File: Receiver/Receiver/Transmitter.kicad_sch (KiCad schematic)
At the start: 72 parts, among them J1 SSW-104-01-T-D-LL, J10 Conn_01x03, J11 Conn_01x03, J12 Conn_01x03, J13 Conn_01x03, J14 Conn_01x03, J2 105-1103-001, J3 Conn_01x06, J4 105-1103-001, J5 105-1103-001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

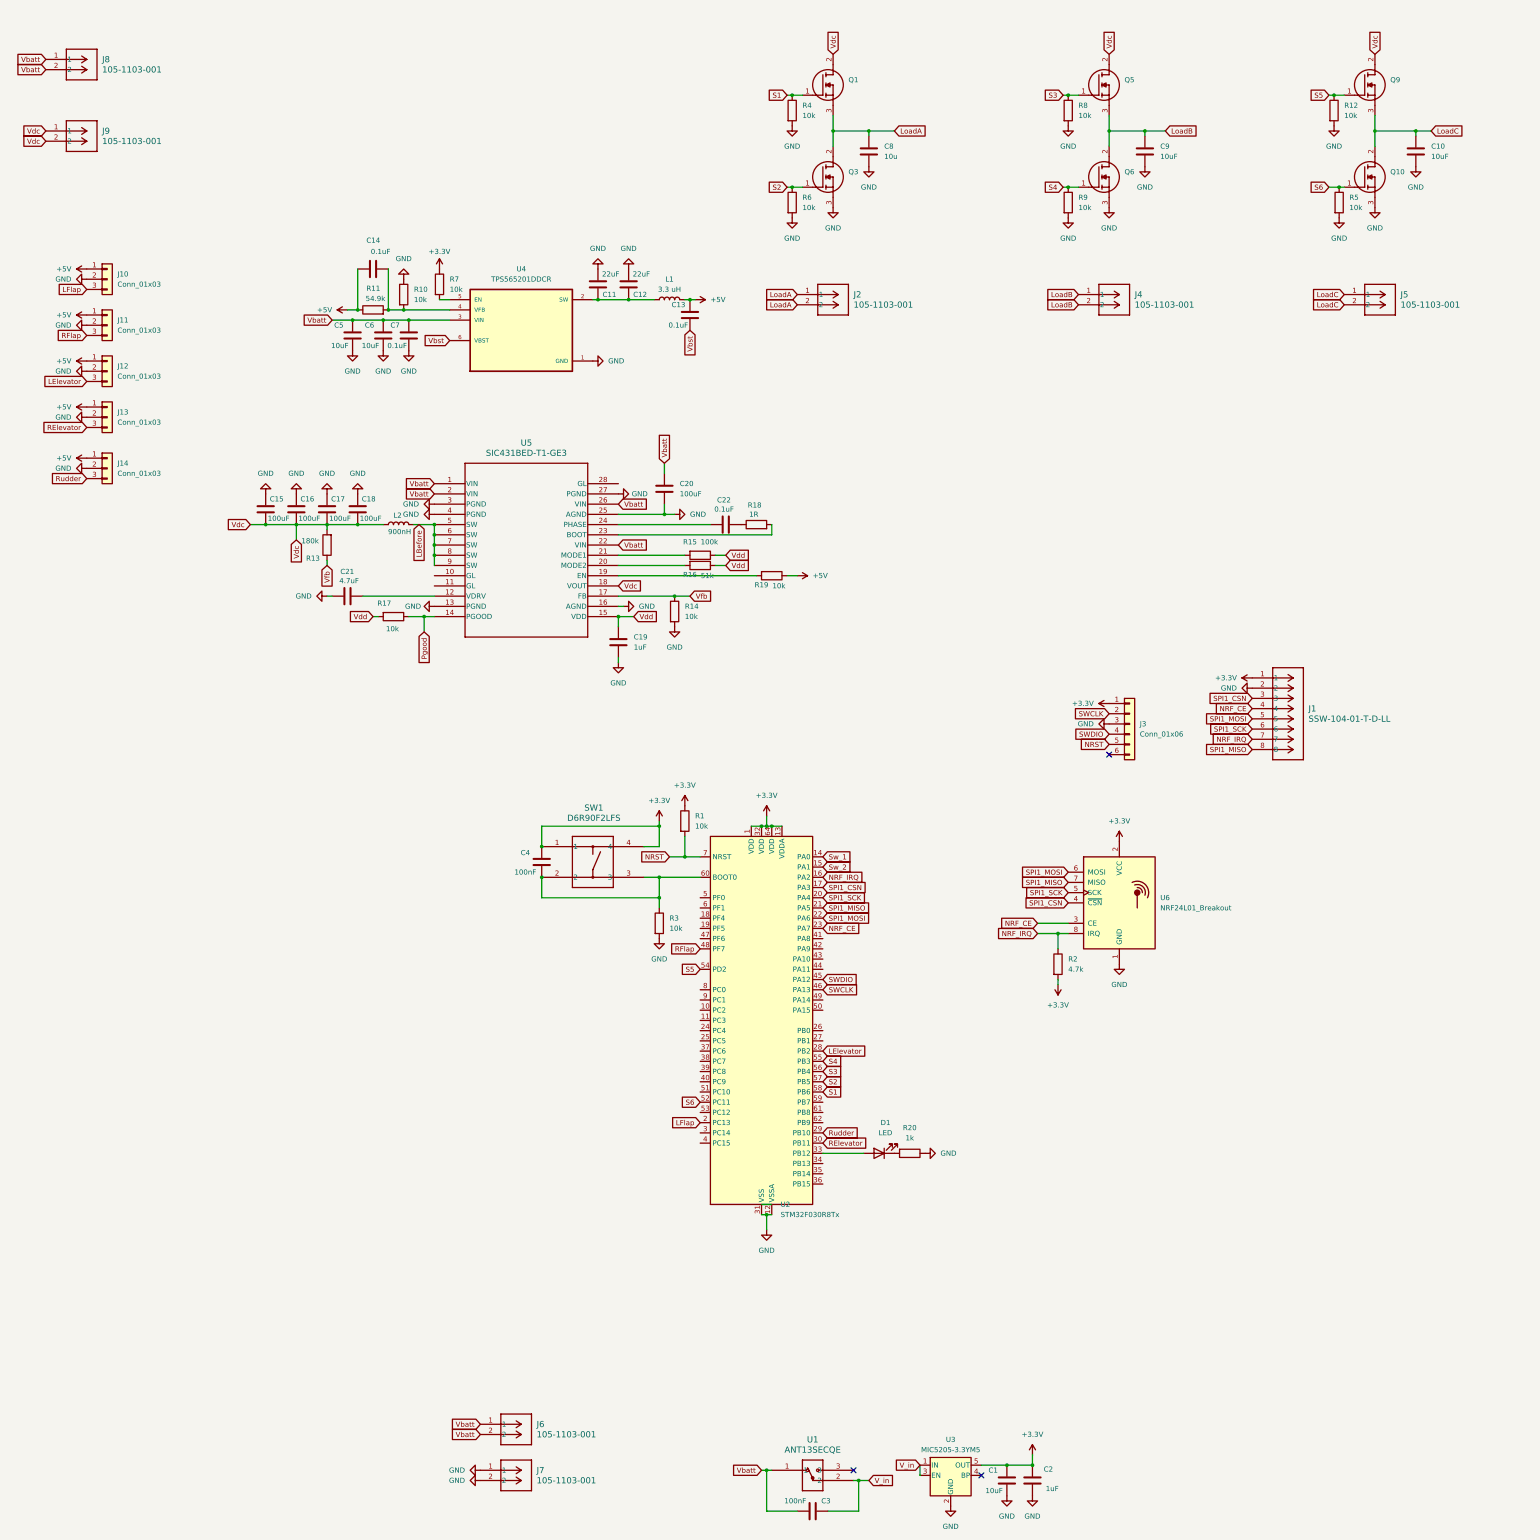
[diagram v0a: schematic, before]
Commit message: Updated KICAD files for V1, corrected SWDIO header
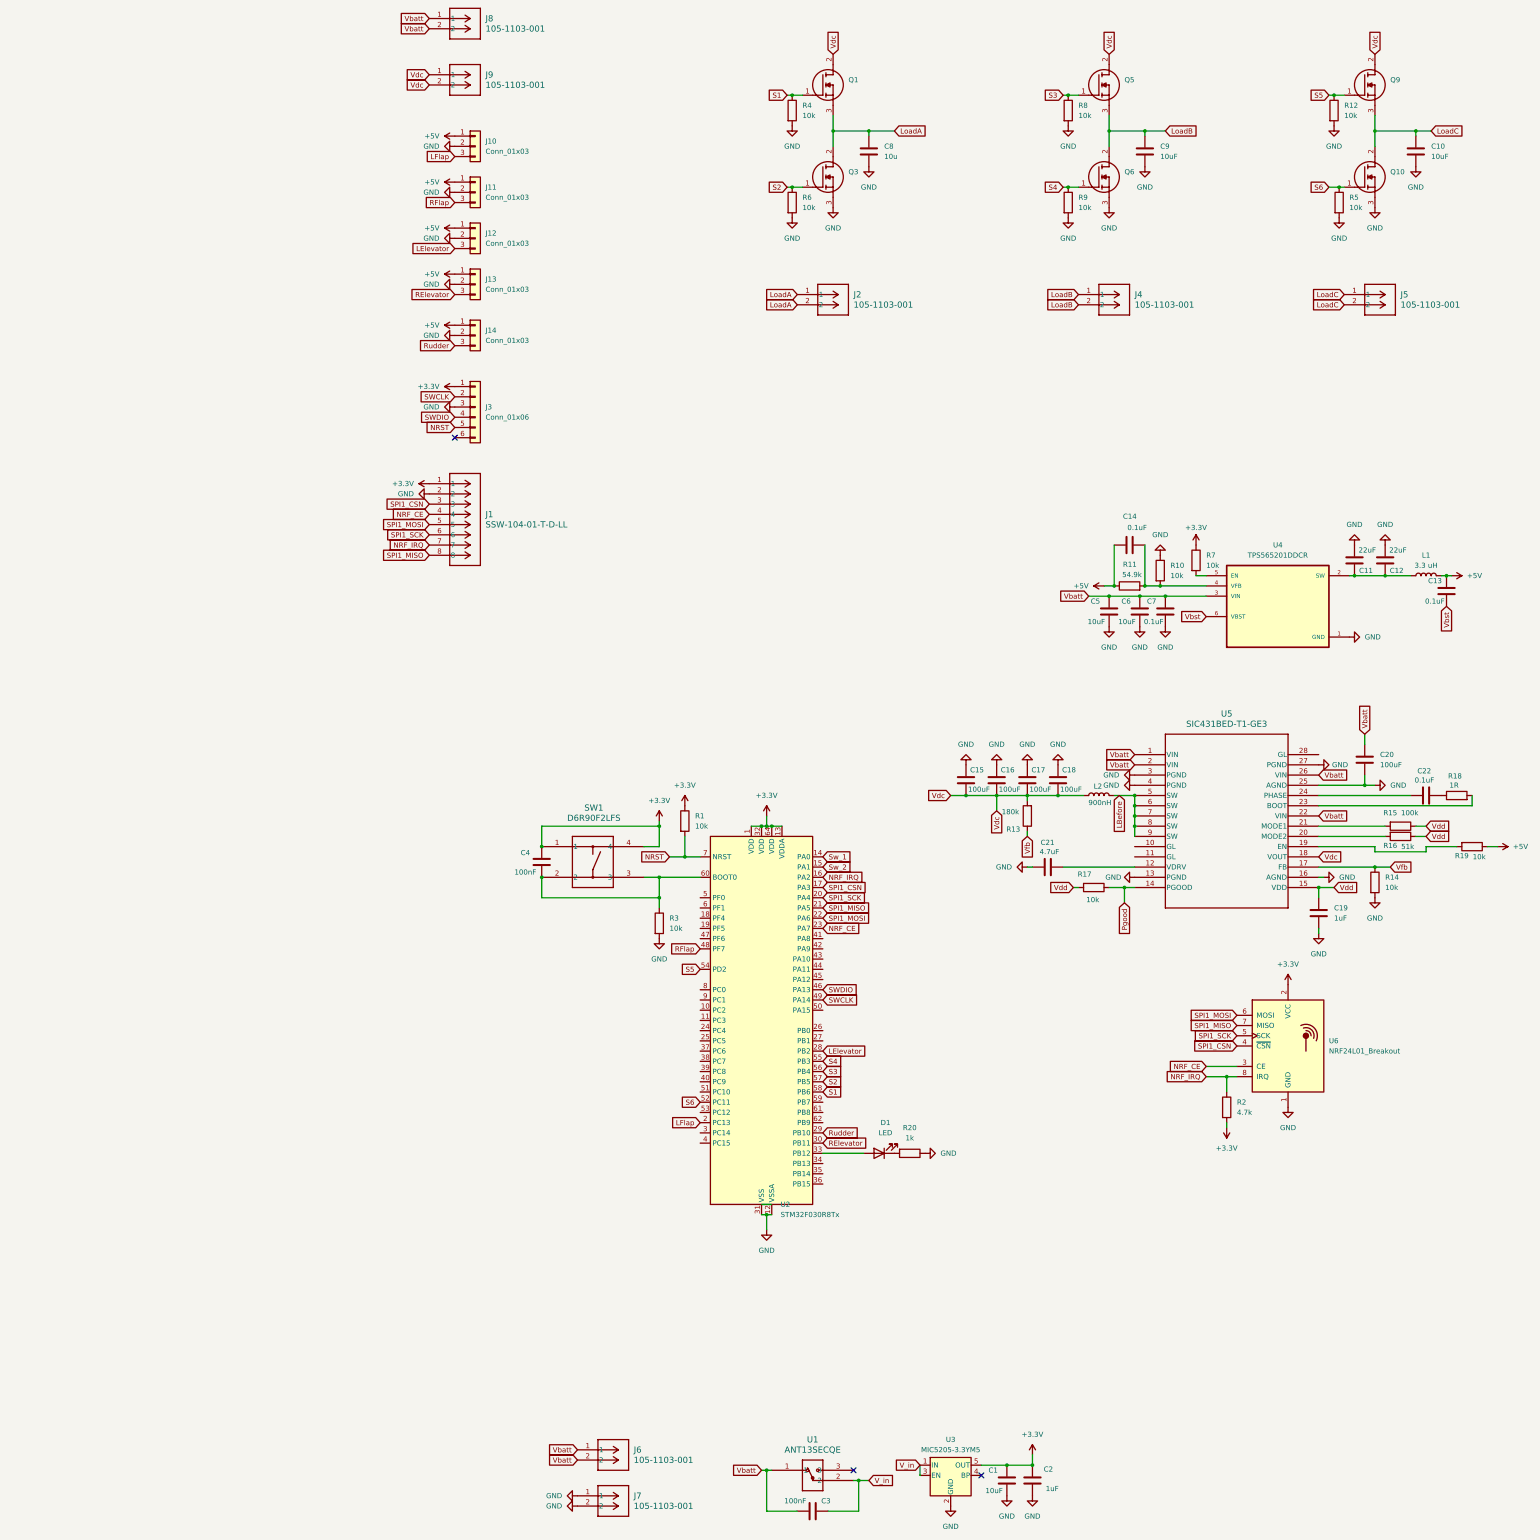
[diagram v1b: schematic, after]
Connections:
- net SWCLK: now also U2.49 (PA14); no longer U2.46 (PA13)
- net SWDIO: now also U2.46 (PA13); no longer U2.45 (PA12)
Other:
- moved on the sheet: C11, C12, C13, C14, C15, C16, C17, C18, C19, C20, C21, C22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

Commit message: PCB V2 updates
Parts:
- removed C3: 100nF, Capacitor_SMD:C_0402_1005Metric, symbol Device:C
- removed J6, J7, J8, J9: 105-1103-001, Libary1:CONN_105-1102-001, symbol BananaPlug:105-1103-001
- added C23: 0.1uF, Capacitor_SMD:C_0402_1005Metric, symbol Device:C
- added J8, J9: FCR7350R, CONN1_FCR7350R_CLF, symbol FCR7350R:FCR7350R
- added SW2: 500SSP1S2M2QEA, 500SSP1_EWI, symbol 500SSP1S2M2QEA:500SSP1S2M2QEA
- added U7: HEF4104BT_653, SO16_SOT109-1_NEX, symbol HEF4104BT:HEF4104BT_653
- C21: value 4.7uF -> 10uF
- C4: value 100nF -> 0.1uF
- R2: value 4.7k -> 10k
- U1: footprint Library2:ANT13SEC_CRS -> ANT13SEC_CRS
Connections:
- net +3.3V: now also U7.16 (VDD(A))
- net +5V: now also J10.2 (Pin_2), J11.2 (Pin_2), J12.2 (Pin_2), J13.2 (Pin_2), J14.2 (Pin_2); no longer J10.1 (Pin_1), J11.1 (Pin_1), J12.1 (Pin_1), J13.1 (Pin_1), J14.1 (Pin_1)
- net GND: now also J10.1 (Pin_1), J11.1 (Pin_1), J12.1 (Pin_1), J13.1 (Pin_1), J14.1 (Pin_1), J8.1, U7.8 (VSS); no longer J10.2 (Pin_2), J11.2 (Pin_2), J12.2 (Pin_2), J13.2 (Pin_2), J14.2 (Pin_2)
- net S1: now also U7.4 (A0); no longer Q1.1 (G), R4.1
- net S3: now also U7.5 (A1); no longer Q5.1 (G), R8.1
- net S5: now also U7.11 (A2); no longer Q9.1 (G), R12.1
- net V_in: now also C23.2
- net Vbatt: now also C23.1, J9.1, SW2.1
- net Vdc: now also SW2.2, U7.1 (VDD({B))
- net DRIVER_ENABLE: now reaches U2.41 (PA8)
- net DRIVER_ENABLE: now also U7.15 (OE)
- new net S1_BOOSTED: Q1.1 (G), R4.1, U7.3 (B0)
- new net S3_BOOSTED: Q5.1 (G), R8.1, U7.6 (B1)
- new net S5_BOOSTED: Q9.1 (G), R12.1, U7.10 (B2)
- no-connect marks 3 -> 10
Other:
- moved on the sheet: C1, C2, U3

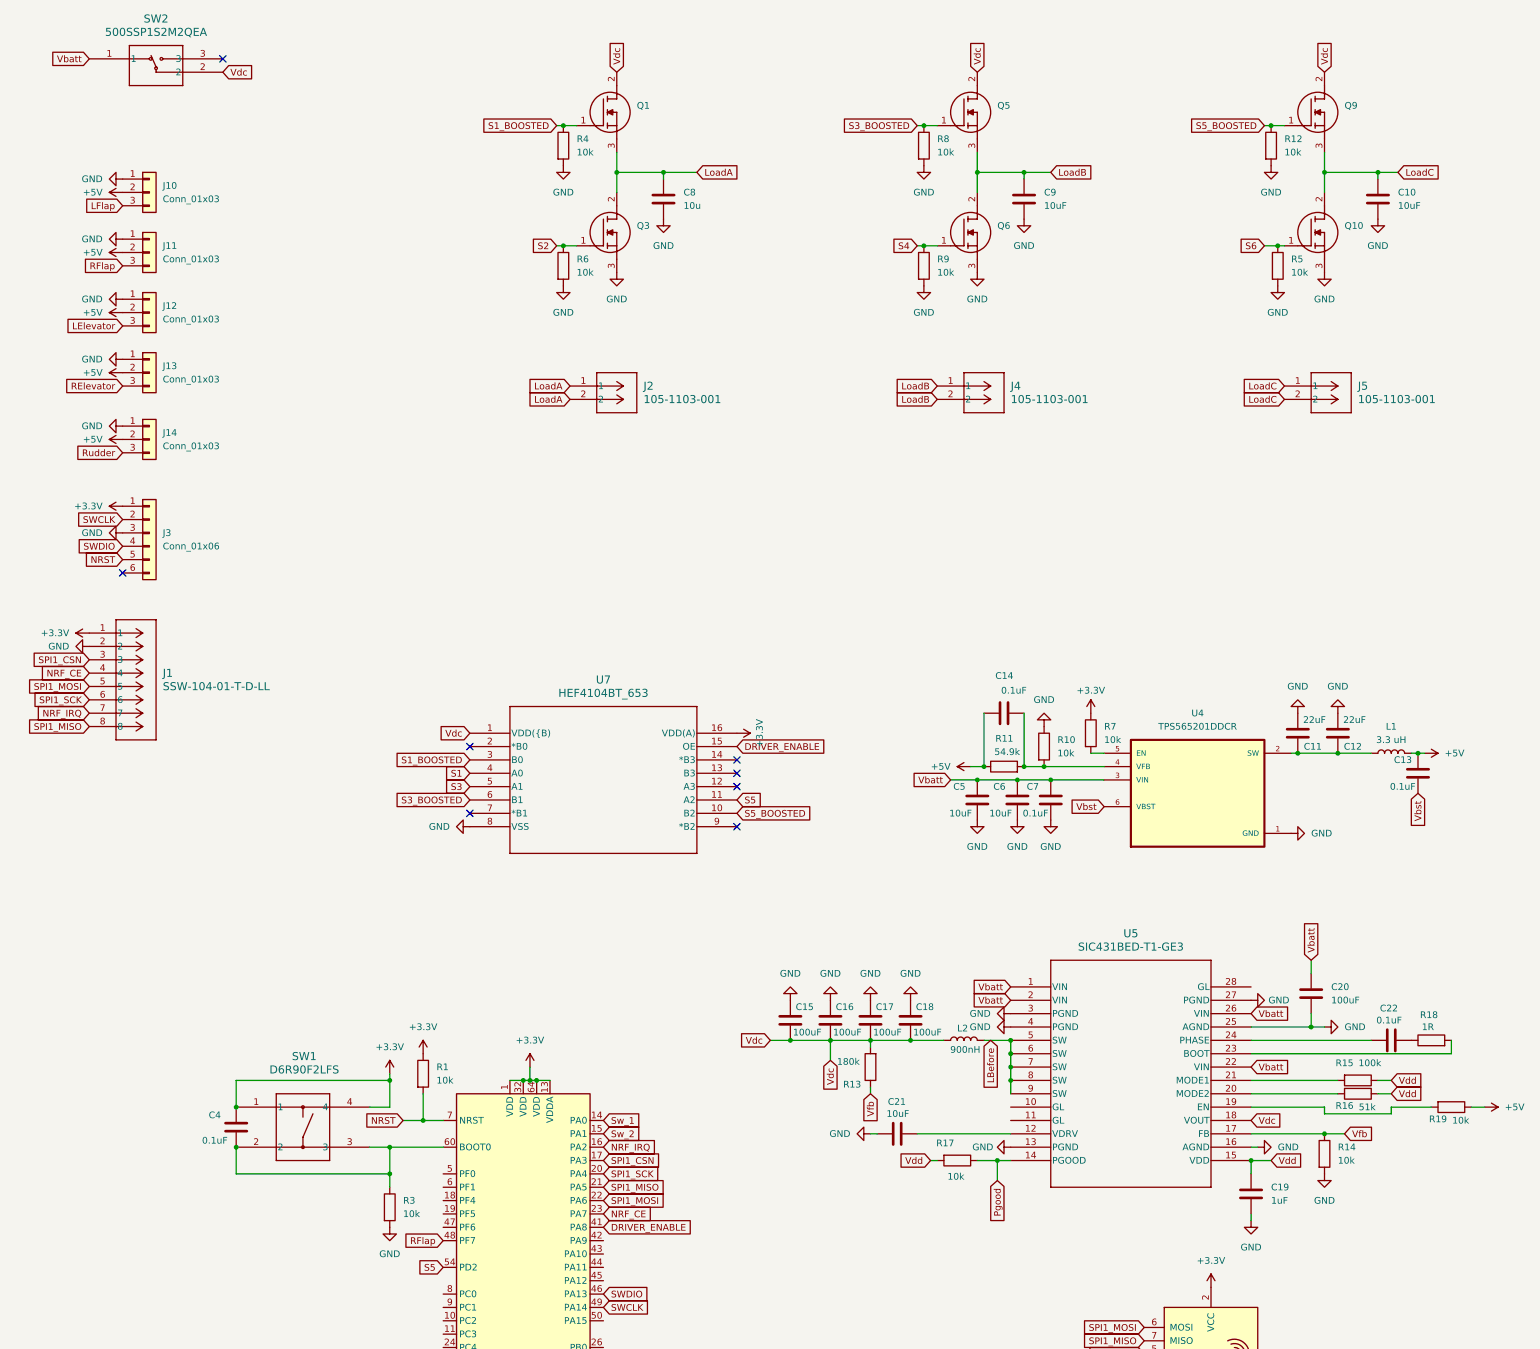
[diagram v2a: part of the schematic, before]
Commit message: Removed extra voltage converter and rerouted PCB
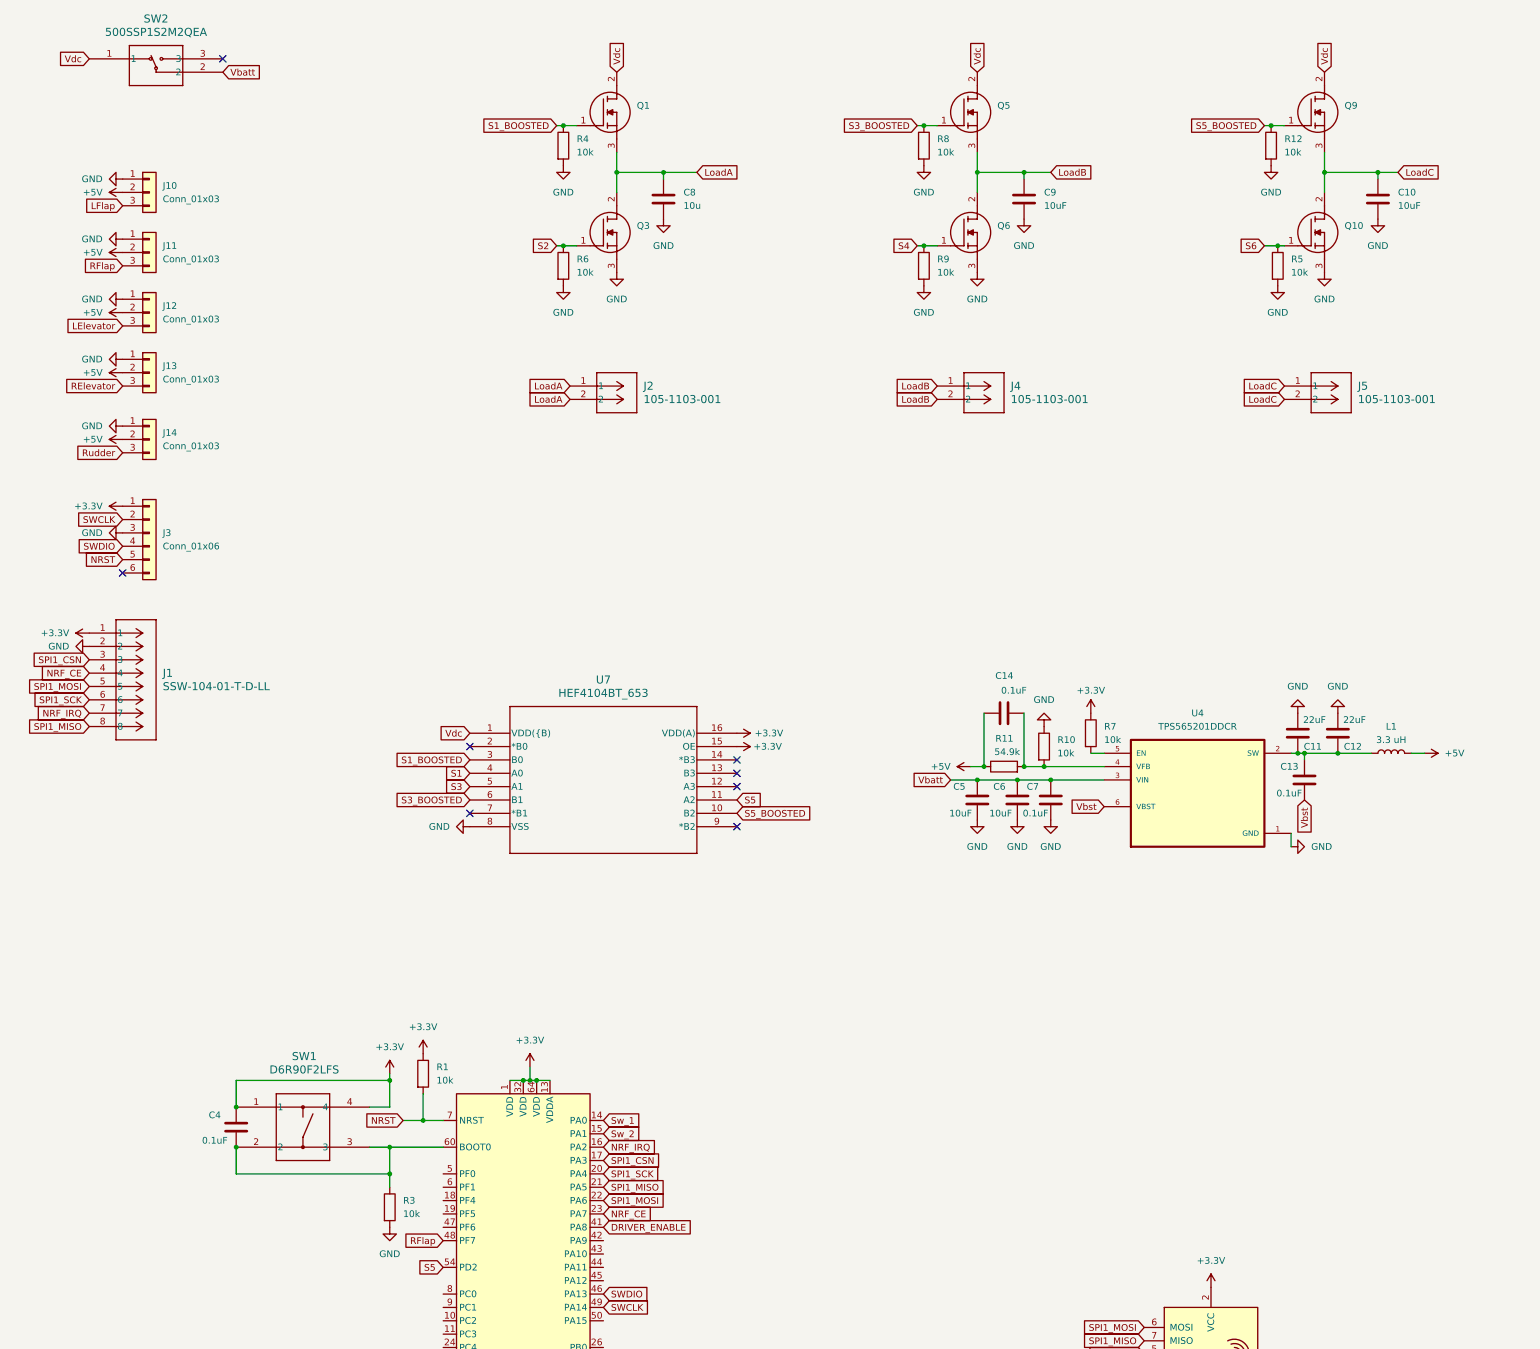
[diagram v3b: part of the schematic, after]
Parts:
- removed C15, C16, C17, C18, C20: 100uF, Libary1:100uFCap, symbol Device:C
- removed C19: 1uF, Capacitor_SMD:C_0603_1608Metric, symbol Device:C
- removed C21: 10uF, Capacitor_SMD:C_0603_1608Metric, symbol Device:C
- removed C22: 0.1uF, Capacitor_SMD:C_0402_1005Metric, symbol Device:C
- removed L2: 900nH, Inductor_SMD:L_1206_3216Metric, symbol Device:L
- removed R13: 180k, Resistor_SMD:R_1206_3216Metric, symbol Device:R
- removed R14, R17, R19: 10k, Resistor_SMD:R_0603_1608Metric, symbol Device:R
- removed R15: 100k, Resistor_SMD:R_1206_3216Metric, symbol Device:R
- removed R16: 51k, Resistor_SMD:R_1206_3216Metric, symbol Device:R
- removed R18: 1R, Resistor_SMD:R_0402_1005Metric, symbol Device:R
- removed U5: SIC431BED-T1-GE3, Libary1:QFN_ED-T1-GE3_VIS, symbol BatteryVoltageRegulator:SIC431BED-T1-GE3
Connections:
- net +3.3V: now also U7.15 (OE)
- net +5V: no longer C13.1
- net DRIVER_ENABLE: no longer U7.15 (OE)
- net Vbatt: now also SW2.2; no longer SW2.1
- net Vdc: now also SW2.1; no longer SW2.2
- net at C11.1, C12.1, L1.1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: now also C13.1
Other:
- moved on the sheet: C13
